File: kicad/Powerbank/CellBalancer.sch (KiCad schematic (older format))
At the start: 41 parts

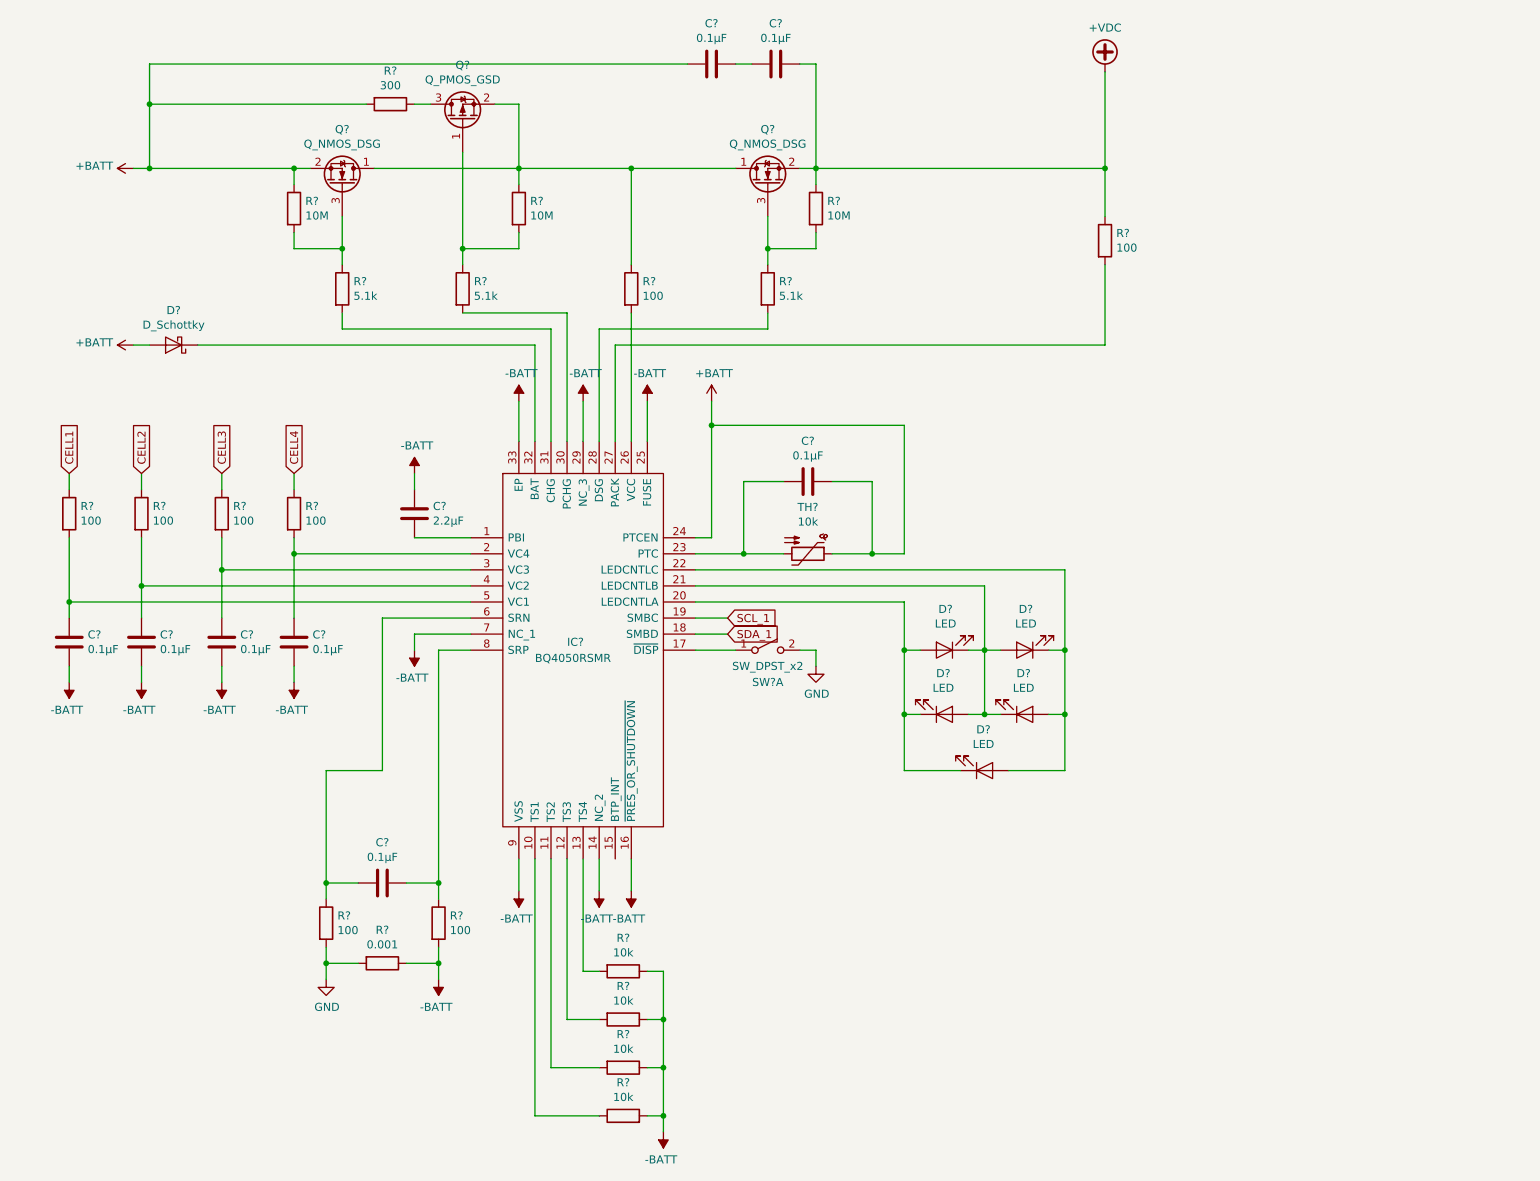
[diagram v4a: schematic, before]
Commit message: Double checked schematic towards reference design
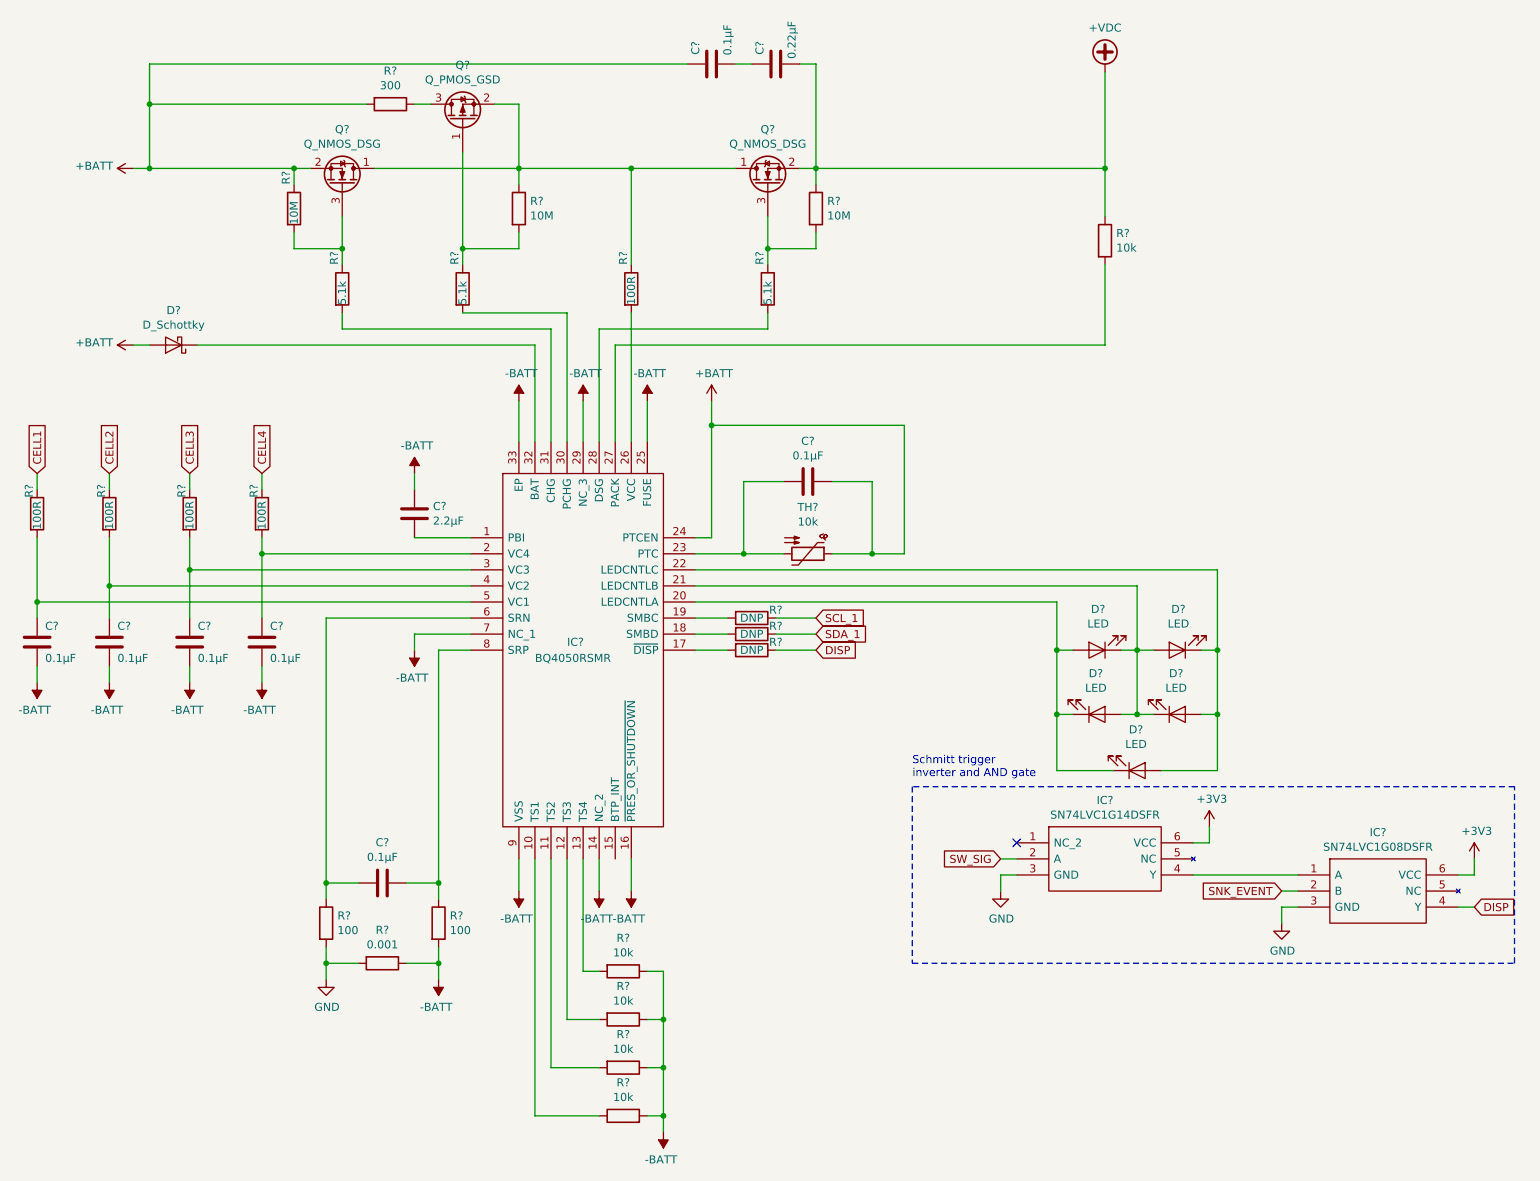
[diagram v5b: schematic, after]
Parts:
- removed SW?: SW_DPST_x2, symbol Switch:SW_DPST_x2
- added IC?: SN74LVC1G08DSFR, SON35P100X100X40-6N, symbol Powerbank:SN74LVC1G08DSFR
- added IC?: SN74LVC1G14DSFR, SON35P100X100X40-6N, symbol Powerbank:SN74LVC1G14DSFR
- added R? (x3): DNP, symbol Device:R
- C?: value 0.1µF -> 0.22µF
- R? (x5): value 100 -> 100R
- R?: value 100 -> 10k
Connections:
- net GND: now also IC?.3 (GND), IC?.3 (GND)
- net SCL_1: now also R?.1; no longer IC?.19 (SMBC)
- net SDA_1: now also R?.1; no longer IC?.18 (SMBD)
- net at IC?.17 (~DISP): now also R?.2
- new net: IC?.18 (SMBD), R?.2
- new net: IC?.19 (SMBC), R?.2
- new net: IC?.1 (A), IC?.4 (Y)
- new net +3V3: IC?.6 (VCC), IC?.6 (VCC)
- new net DISP: IC?.4 (Y), R?.1
- new net SNK_EVENT: IC?.2 (B)
- new net SW_SIG: IC?.2 (A)
- no-connect marks 0 -> 1
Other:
- note added: "Schmitt trigger \ninverter and AND gate"
- moved on the sheet: C?, D?, R?

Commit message: Updated for PCB
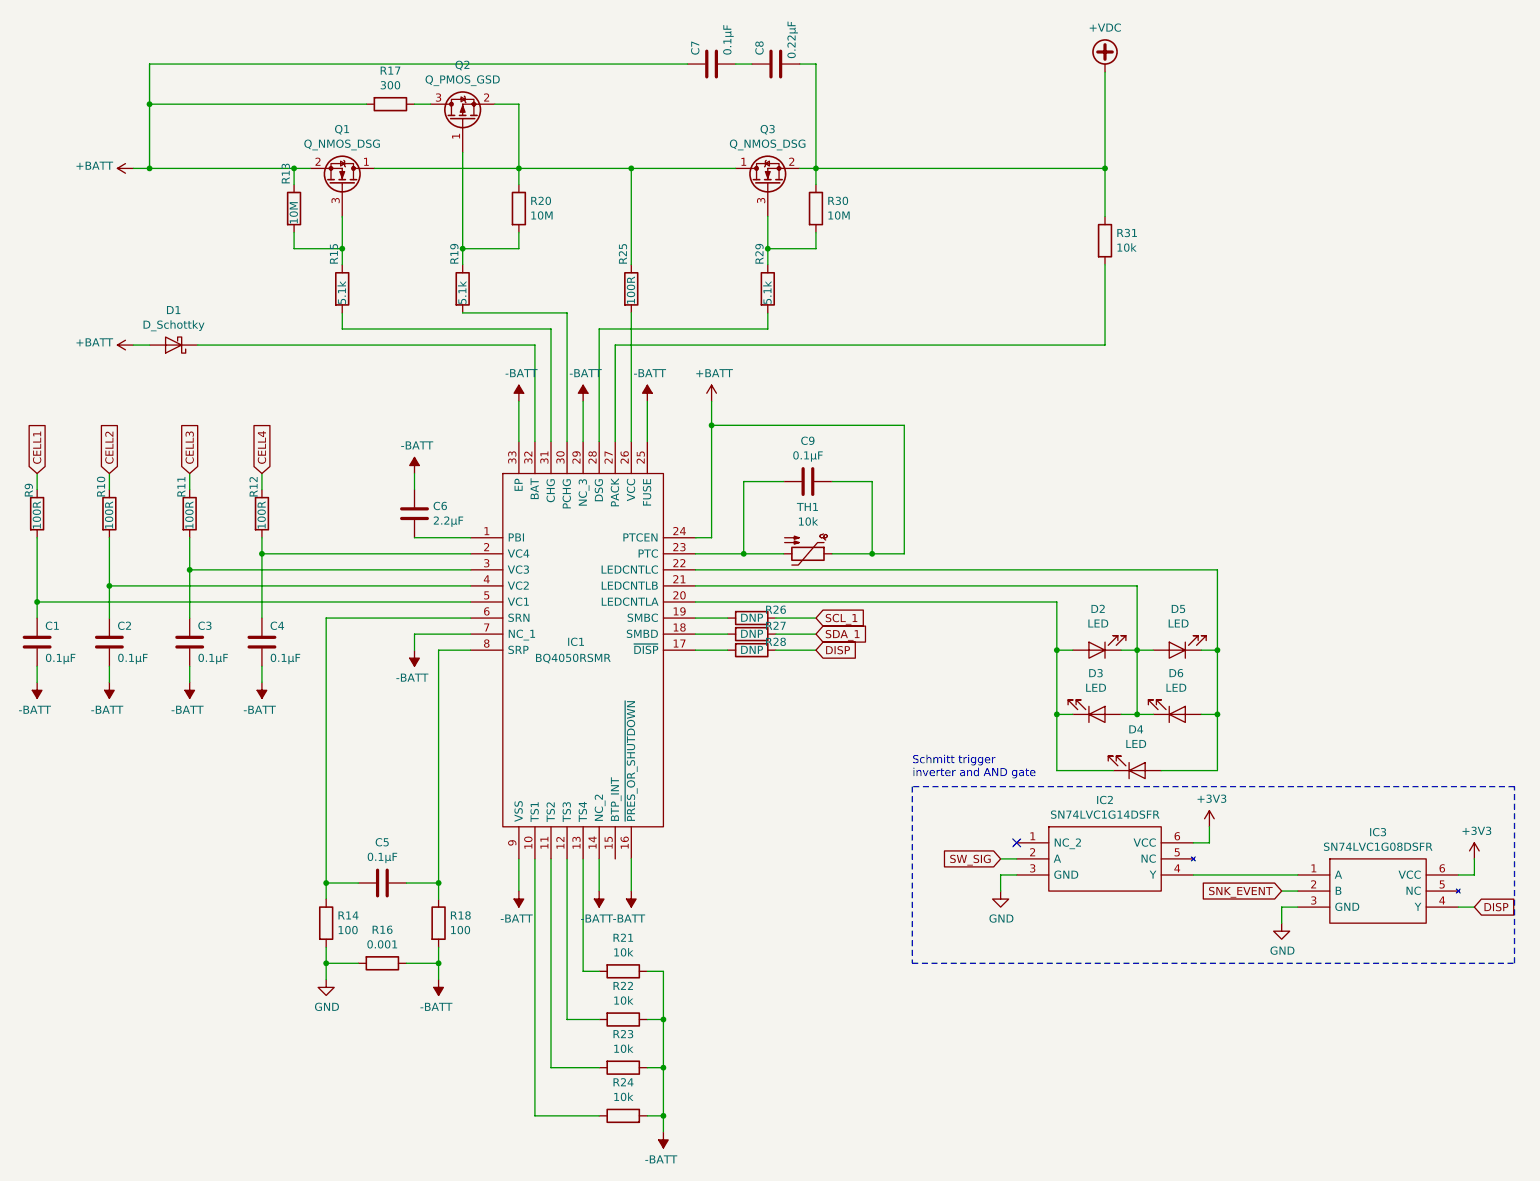
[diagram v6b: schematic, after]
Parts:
- C1, C2, C3, C4, C5, C6, C7, C8, C9: renamed from C?; footprint (none) -> Capacitor_SMD:C_0603_1608Metric
- D2, D3, D4, D5, D6: renamed from D?; footprint (none) -> LED_SMD:LED_0603_1608Metric
- IC1: renamed from IC?; footprint QFN40P400X400X100-33N-D -> Powerbank:QFN40P400X400X100-33N-D
- IC2, IC3: renamed from IC?; footprint SON35P100X100X40-6N -> (none)
- R10, R11, R12, R13, R14, R15, R16, R17, R18, R19, R20, R21, R22, R23, R24, R25, R26, R27, R28, R29, R30, R31, R9: renamed from R?; footprint (none) -> Resistor_SMD:R_0603_1608Metric
- gave numbers to parts that had none: 5

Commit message: Added footprint for all, moved to a first attempt for routing
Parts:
- removed Q1, Q3: Q_NMOS_DSG, symbol Device:Q_NMOS_DSG
- removed Q2: Q_PMOS_GSD, symbol Device:Q_PMOS_GSD
- added Q1, Q3: Q_NMOS_GDS, Package_TO_SOT_SMD:TO-252-3_TabPin2, symbol Device:Q_NMOS_GDS
- added Q2: Q_PMOS_GDS, Package_TO_SOT_SMD:TO-252-2, symbol Device:Q_PMOS_GDS
- D1: footprint (none) -> Diode_SMD:D_SOD-523
- IC2, IC3: footprint (none) -> Package_TO_SOT_SMD:SOT-23-5
- R16: footprint Resistor_SMD:R_0603_1608Metric -> Resistor_SMD:R_1206_3216Metric
- R26, R27, R28: footprint Resistor_SMD:R_0603_1608Metric -> Resistor_SMD:R_0201_0603Metric
- TH1: footprint (none) -> Resistor_SMD:R_0402_1005Metric
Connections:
- net +BATT: now also Q1.3 (S)
- net +VDC: now also Q3.3 (S)
- net Source: now reaches R20.1, R25.1
- net Source: now also Q1.2 (D), Q2.3 (S), Q3.2 (D)
- net at R29.1, R30.2: now also Q3.1 (G)
- net at R13.2, R15.1: now also Q1.1 (G)
- net at R19.1, R20.2: now also Q2.1 (G)
- net at R17.1: now also Q2.2 (D)
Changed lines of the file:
@@
 F 0 "R16" V 3893 6500 50  0000 C CNN
 F 1 "0.001" V 3984 6500 50  0000 C CNN
-F 2 "Resistor_SMD:R_0603_1608Metric" V 4030 6500 50  0001 C CNN
+F 2 "Resistor_SMD:R_1206_3216Metric" V 4030 6500 50  0001 C CNN
 F 3 "~" H 4100 6500 50  0001 C CNN
 	1    4100 6500
@@
 F 0 "D1" H 2800 2434 50  0000 C CNN
 F 1 "D_Schottky" H 2800 2525 50  0000 C CNN
-F 2 "" H 2800 2650 50  0001 C CNN
+F 2 "Diode_SMD:D_SOD-523" H 2800 2650 50  0001 C CNN
 F 3 "~" H 2800 2650 50  0001 C CNN
 	1    2800 2650
@@
 F 0 "TH1" V 6460 3950 50  0000 C CNN
 F 1 "10k" V 6551 3950 50  0000 C CNN
-F 2 "" H 6800 3750 50  0001 L CNN
+F 2 "Resistor_SMD:R_0402_1005Metric" H 6800 3750 50  0001 L CNN
 F 3 "~" H 6750 3950 50  0001 C CNN
 	1    6750 3950
@@
 	5350 3000 5350 3250
 $Comp
-L Device:Q_NMOS_DSG Q3
-U 1 1 5E1C65B2
-P 6500 1650
-F 0 "Q3" V 6843 1650 50  0000 C CNN
-F 1 "Q_NMOS_DSG" V 6752 1650 50  0000 C CNN
-F 2 "" H 6700 1750 50  0001 C CNN
-F 3 "~" H 6500 1650 50  0001 C CNN
-	1    6500 1650
-	0    -1   -1   0
-$EndComp
-$Comp
-L Device:Q_NMOS_DSG Q1
-U 1 1 5E1D600F
-P 3850 1650
-F 0 "Q1" V 4193 1650 50  0000 C CNN
-F 1 "Q_NMOS_DSG" V 4102 1650 50  0000 C CNN
-F 2 "" H 4050 1750 50  0001 C CNN
-F 3 "~" H 3850 1650 50  0001 C CNN
-	1    3850 1650
-	0    1    -1   0
-$EndComp
-$Comp
-L Device:Q_PMOS_GSD Q2
-U 1 1 5E1D7A90
-P 4600 1250
-F 0 "Q2" V 4943 1250 50  0000 C CNN
-F 1 "Q_PMOS_GSD" V 4852 1250 50  0000 C CNN
-F 2 "" H 4800 1350 50  0001 C CNN
-F 3 "~" H 4600 1250 50  0001 C CNN
-	1    4600 1250
-	0    -1   -1   0
-$EndComp
-$Comp
 L Device:R R30
 U 1 1 5E1D9C71
@@
 F 0 "R26" V 6350 4500 50  0000 C CNN
 F 1 "DNP" V 6400 4350 50  0000 C CNN
-F 2 "Resistor_SMD:R_0603_1608Metric" V 6330 4350 50  0001 C CNN
+F 2 "Resistor_SMD:R_0201_0603Metric" V 6330 4350 50  0001 C CNN
 F 3 "~" H 6400 4350 50  0001 C CNN
 	1    6400 4350
@@
 F 0 "R27" V 6350 4600 50  0000 C CNN
 F 1 "DNP" V 6400 4450 50  0000 C CNN
-F 2 "Resistor_SMD:R_0603_1608Metric" V 6330 4450 50  0001 C CNN
+F 2 "Resistor_SMD:R_0201_0603Metric" V 6330 4450 50  0001 C CNN
 F 3 "~" H 6400 4450 50  0001 C CNN
 	1    6400 4450
@@
 F 0 "IC3" H 10300 6215 50  0000 C CNN
 F 1 "SN74LVC1G08DSFR" H 10300 6124 50  0000 C CNN
-F 2 "" H 10650 6050 50  0001 L CNN
+F 2 "Package_TO_SOT_SMD:SOT-23-5" H 10650 6050 50  0001 L CNN
 F 3 "http://www.ti.com/lit/gpn/sn74lvc1g08" H 10650 5950 50  0001 L CNN
 F 4 "SINGLE 2-INPUT POSITIVE-AND GATE" H 10650 5850 50  0001 L CNN "Description"
@@
 F 0 "R28" V 6350 4700 50  0000 C CNN
 F 1 "DNP" V 6400 4550 50  0000 C CNN
-F 2 "Resistor_SMD:R_0603_1608Metric" V 6330 4550 50  0001 C CNN
+F 2 "Resistor_SMD:R_0201_0603Metric" V 6330 4550 50  0001 C CNN
 F 3 "~" H 6400 4550 50  0001 C CNN
 	1    6400 4550
@@
 F 0 "IC2" H 8600 6015 50  0000 C CNN
 F 1 "SN74LVC1G14DSFR" H 8600 5924 50  0000 C CNN
-F 2 "" H 9000 5850 50  0001 L CNN
+F 2 "Package_TO_SOT_SMD:SOT-23-5" H 9000 5850 50  0001 L CNN
 F 3 "http://www.ti.com/lit/gpn/sn74lvc1g14" H 9000 5750 50  0001 L CNN
 F 4 "Texas Instruments SN74LVC1G14DSFR, Schmitt Trigger Inverter, 32mA, 1.65  5.5 V, 6-Pin SON" H 9000 5650 50  0001 L CNN "Description"
@@
 Text Notes 7400 5350 0    50   ~ 0
 Schmitt trigger \ninverter and AND gate
+$Comp
+L Device:Q_PMOS_GDS Q2
+U 1 1 5E11D2B1
+P 4600 1250
+F 0 "Q2" V 4943 1250 50  0000 C CNN
+F 1 "Q_PMOS_GDS" V 4852 1250 50  0000 C CNN
+F 2 "Package_TO_SOT_SMD:TO-252-2" H 4800 1350 50  0001 C CNN
+F 3 "~" H 4600 1250 50  0001 C CNN
+	1    4600 1250
+	0    -1   -1   0
+$EndComp
+Text Label 4800 1150 0    50   ~ 0
+Source
+$Comp
+L Device:Q_NMOS_GDS Q3
+U 1 1 5E1301FE
+P 6500 1650
+F 0 "Q3" V 6843 1650 50  0000 C CNN
+F 1 "Q_NMOS_GDS" V 6752 1650 50  0000 C CNN
+F 2 "Package_TO_SOT_SMD:TO-252-3_TabPin2" H 6700 1750 50  0001 C CNN
+F 3 "~" H 6500 1650 50  0001 C CNN
+	1    6500 1650
+	0    -1   -1   0
+$EndComp
+$Comp
+L Device:Q_NMOS_GDS Q1
+U 1 1 5E1323EB
+P 3850 1650
+F 0 "Q1" V 4193 1650 50  0000 C CNN
+F 1 "Q_NMOS_GDS" V 4102 1650 50  0000 C CNN
+F 2 "Package_TO_SOT_SMD:TO-252-3_TabPin2" H 4050 1750 50  0001 C CNN
+F 3 "~" H 3850 1650 50  0001 C CNN
+	1    3850 1650
+	0    1    -1   0
+$EndComp
 $EndSCHEMATC

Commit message: Double checked footprint for IC and Mosfets
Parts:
- Q1, Q3: footprint Package_TO_SOT_SMD:TO-252-3_TabPin2 -> Package_TO_SOT_SMD:TO-252-2
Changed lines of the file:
@@
 F 0 "Q3" V 6843 1650 50  0000 C CNN
 F 1 "Q_NMOS_GDS" V 6752 1650 50  0000 C CNN
-F 2 "Package_TO_SOT_SMD:TO-252-3_TabPin2" H 6700 1750 50  0001 C CNN
+F 2 "Package_TO_SOT_SMD:TO-252-2" H 6700 1750 50  0001 C CNN
 F 3 "~" H 6500 1650 50  0001 C CNN
 	1    6500 1650
@@
 F 0 "Q1" V 4193 1650 50  0000 C CNN
 F 1 "Q_NMOS_GDS" V 4102 1650 50  0000 C CNN
-F 2 "Package_TO_SOT_SMD:TO-252-3_TabPin2" H 4050 1750 50  0001 C CNN
+F 2 "Package_TO_SOT_SMD:TO-252-2" H 4050 1750 50  0001 C CNN
 F 3 "~" H 3850 1650 50  0001 C CNN
 	1    3850 1650
